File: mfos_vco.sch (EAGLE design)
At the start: 60 parts, among them IC1 TL072P, IC2 TL072P, IC3 TL072P, T1 2N3904, T2 2N3904, U1 POWER, U2 2N5457

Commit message: same problem
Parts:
- D1: device SparkFun-DiscreteSemi:DIODE1N4148 -> SparkFun-DiscreteSemi:DIODEPTH
- R14: value 100k -> 20k
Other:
- moved on the sheet: C1, C10, C2, C3, C4, C5, C6, C7, C8, C9, COARSE, CV1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

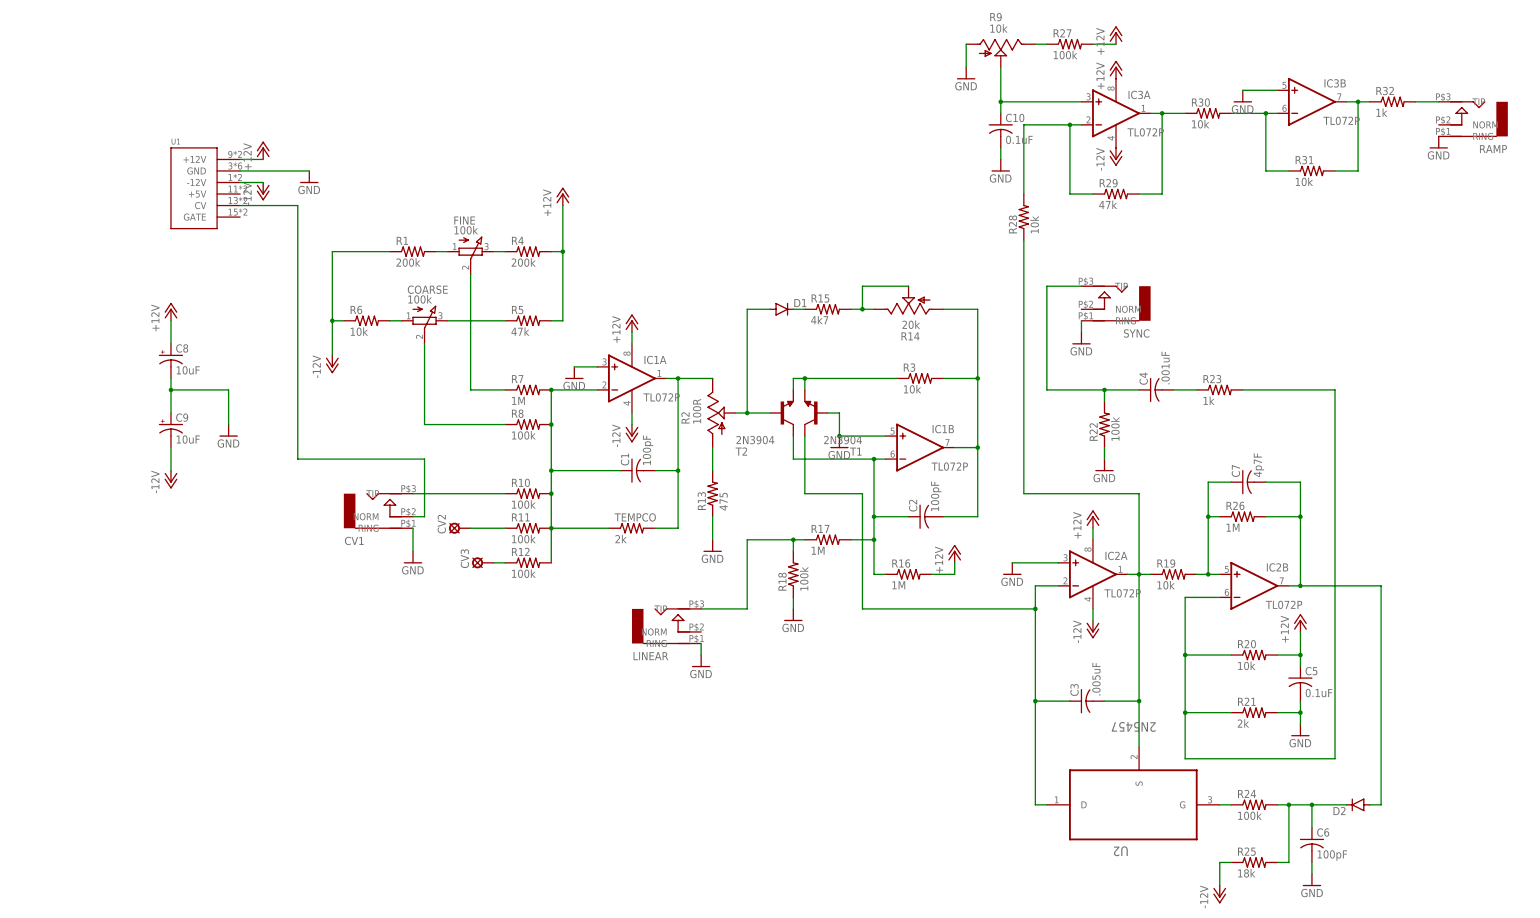
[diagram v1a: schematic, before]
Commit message: changed to mpf102 device to ensure pinout
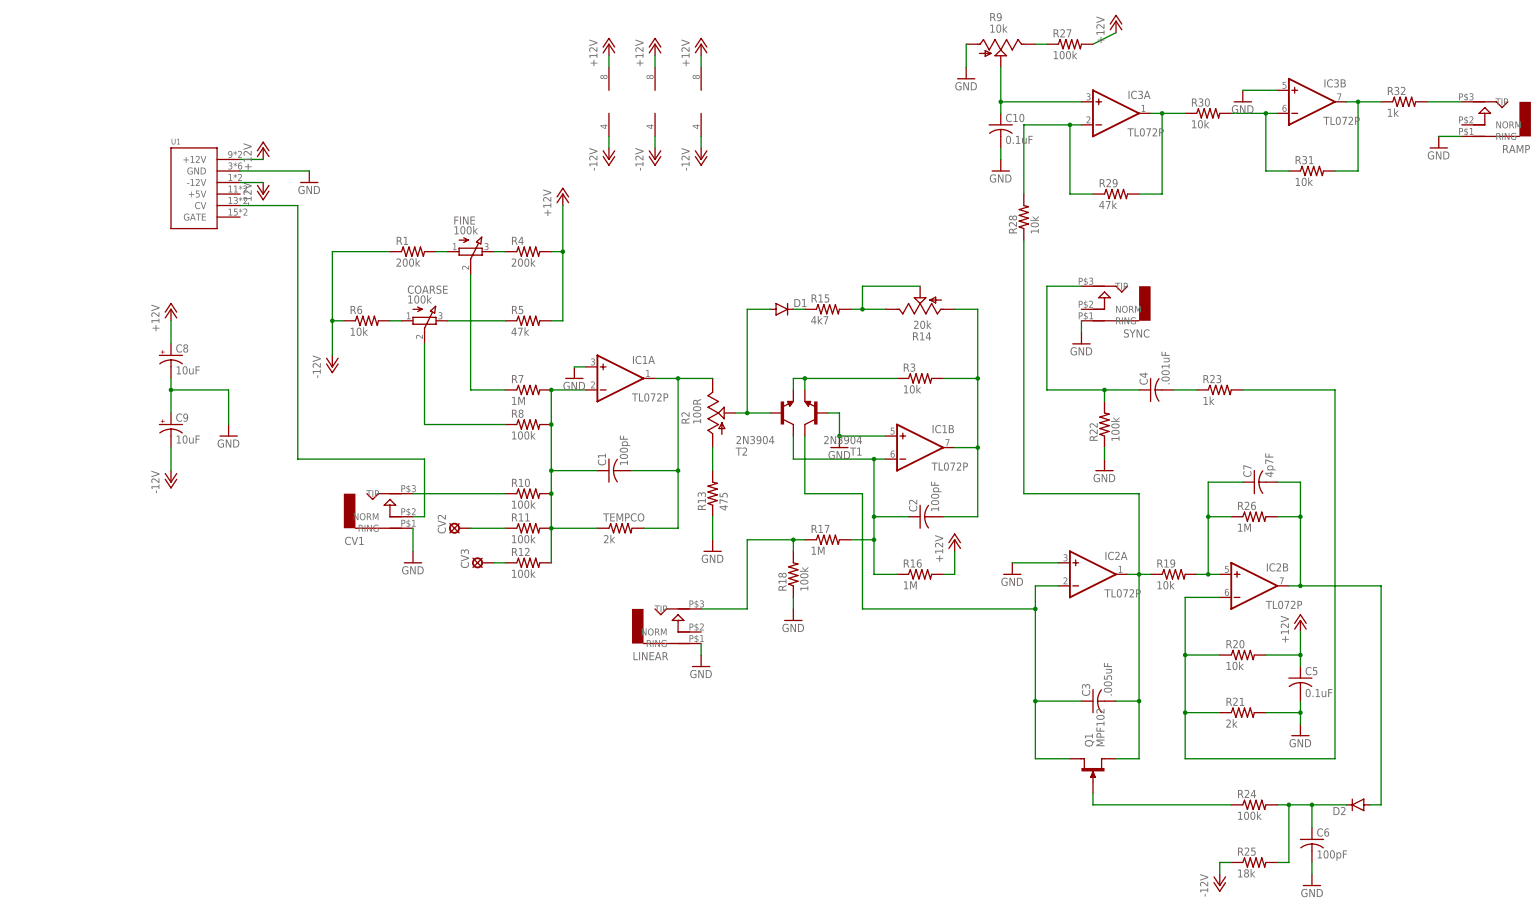
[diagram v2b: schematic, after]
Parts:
- removed U2: 2N5457, Fairchild_By_element14_Batch_1:2N5457
- added Q1: MPF102, bt_transistor:MPF102
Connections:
- net N$21: now also Q1.S; no longer U2.S
- net N$23: now also Q1.D; no longer U2.D
- net N$29: now also Q1.G; no longer U2.G
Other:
- moved on the sheet: C1, C3, C7, IC1A, R14, R16, R20, R21, R26, R32, RAMP, TEMPCO
